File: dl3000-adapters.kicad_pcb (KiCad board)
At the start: 2 copper layers, 57 x 68 mm, 7 parts, among them J1 Banana Jack, J2 BNC, J3 Banana Jack

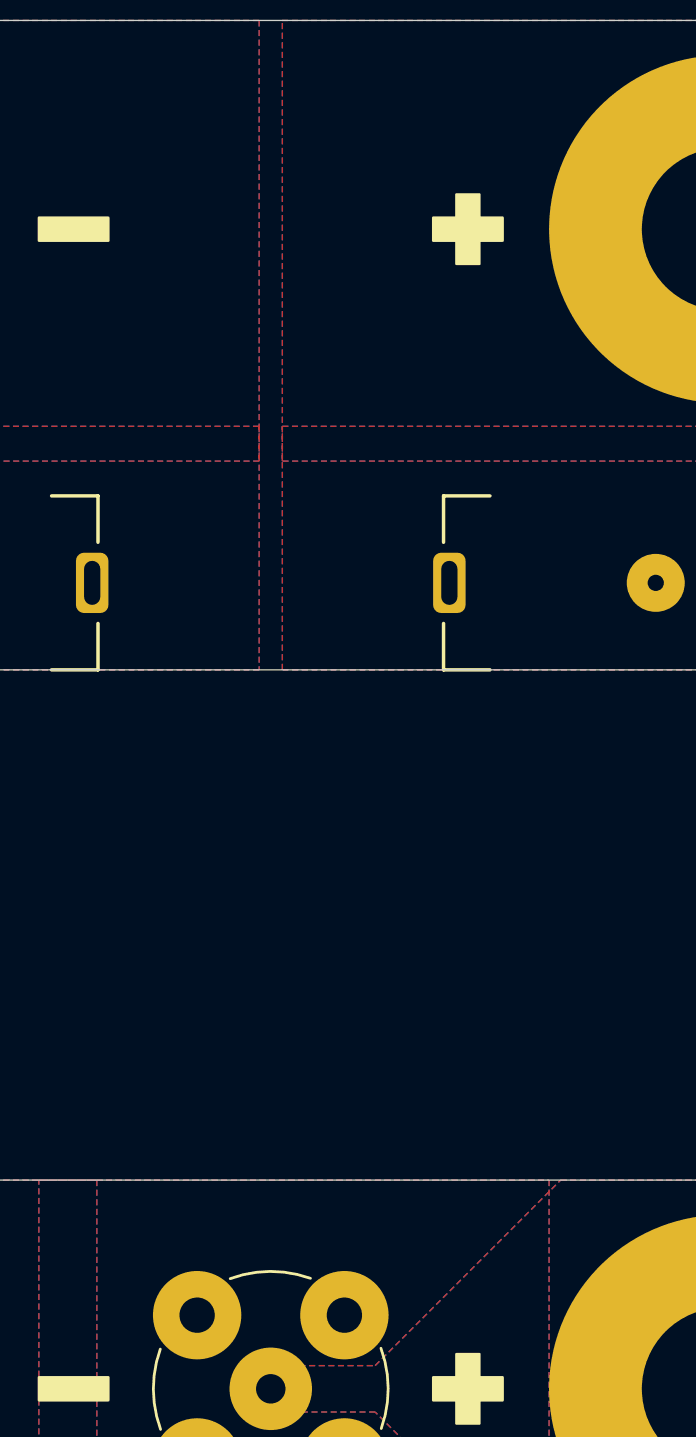
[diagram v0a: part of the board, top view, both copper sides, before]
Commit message: Add high voltage symbols to top silk screen
This includes deriving the very small and ultra small symbol from the
copper layer variant already present in the library.
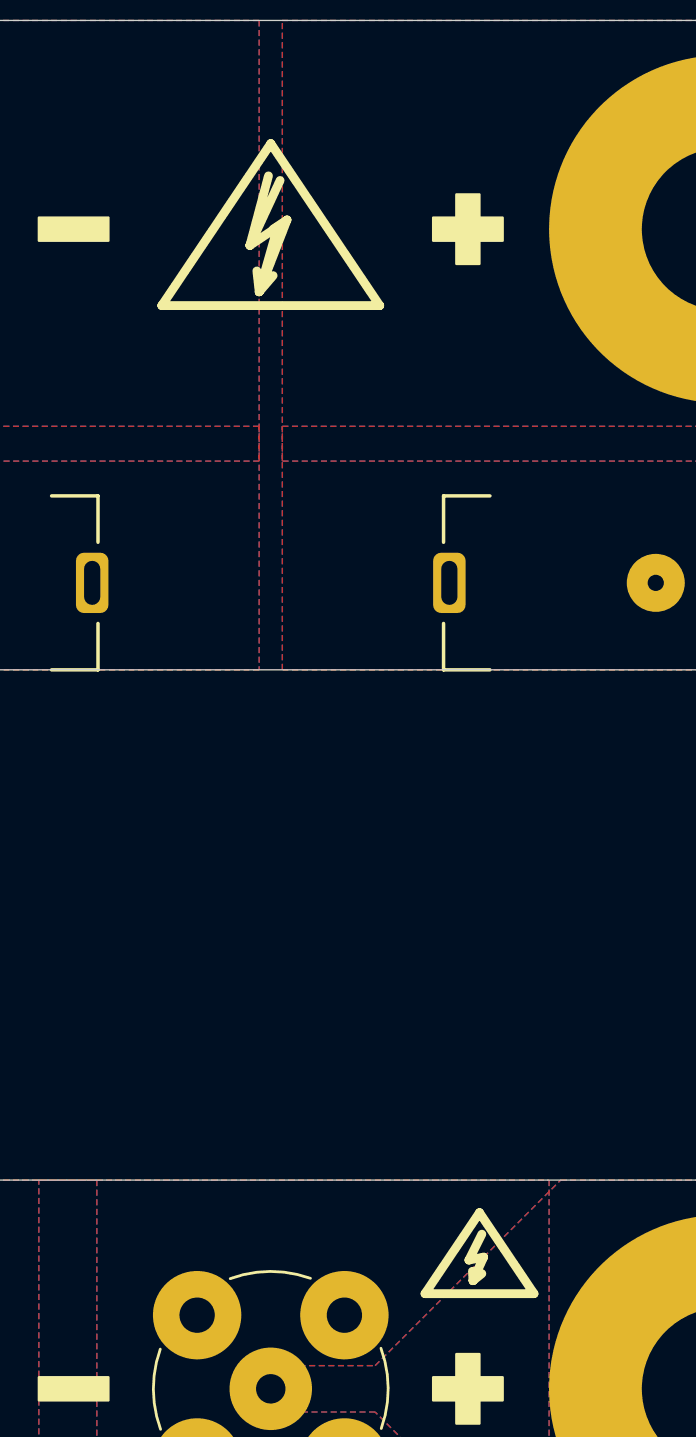
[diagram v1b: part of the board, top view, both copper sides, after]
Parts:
- added REF**: Symbol_HighVoltage_Type2_SilkScreenTop_UltraSmall, Symbol_Local:Symbol_HighVoltage_Type2_SilkScreenTop_UltraSmall, F.Cu at (159.0, 94.5)
- added REF**: Symbol_HighVoltage_Type2_SilkScreenTop_VerySmall, Symbol_Local:Symbol_HighVoltage_Type2_SilkScreenTop_VerySmall, F.Cu at (150.0, 50.5)
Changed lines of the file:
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@@
     (tracks 0)
     (zones 0)
-    (modules 7)
+    (modules 9)
     (nets 5)
   )
@@
     (add_net /BANANA+)
     (add_net /BNC+)
+  )
+  (module Symbol_Local:Symbol_HighVoltage_Type2_SilkScreenTop_UltraSmall (layer F.Cu)
+    (at 159 94.5)
+    (descr "Symbol, High Voltage, Type 2, Copper Top, Very Small,")
+    (tags "Symbol, High Voltage, Type 2, Copper Top, Very Small,")
+    (attr virtual)
+    (fp_text reference REF** (at -0.127 -5.715) (layer F.SilkS) hide
+      (effects (font (size 1 1) (thickness 0.15)))
+    )
+    (fp_text value Symbol_HighVoltage_Type2_SilkScreenTop_UltraSmall (at -0.381 4.572) (layer F.Fab) hide
+      (effects (font (size 1 1) (thickness 0.15)))
+    )
+    (fp_line (start -0.2794 0.8382) (end 0.1016 0.5334) (layer F.SilkS) (width 0.381))
+    (fp_line (start -0.3048 0.4318) (end -0.2794 0.8382) (layer F.SilkS) (width 0.381))
+    (fp_line (start 0.1778 -0.1778) (end -0.2794 0.8382) (layer F.SilkS) (width 0.381))
+    (fp_line (start -0.4572 -0.0508) (end 0.1778 -0.1778) (layer F.SilkS) (width 0.381))
+    (fp_line (start 0.1016 -1.1684) (end -0.4572 -0.0508) (layer F.SilkS) (width 0.381))
+    (fp_line (start 0 -2.0955) (end 2.3495 1.397) (layer F.SilkS) (width 0.381))
+    (fp_line (start 2.3495 1.397) (end -2.3495 1.397) (layer F.SilkS) (width 0.381))
+    (fp_line (start -2.3495 1.397) (end 0 -2.0955) (layer F.SilkS) (width 0.381))
+  )
+  (module Symbol_Local:Symbol_HighVoltage_Type2_SilkScreenTop_VerySmall (layer F.Cu)
+    (at 150 50.5)
+    (descr "Symbol, High Voltage, Type 2, Copper Top, Very Small,")
+    (tags "Symbol, High Voltage, Type 2, Copper Top, Very Small,")
+    (attr virtual)
+    (fp_text reference REF** (at -0.127 -5.715) (layer F.SilkS) hide
+      (effects (font (size 1 1) (thickness 0.15)))
+    )
+    (fp_text value Symbol_HighVoltage_Type2_SilkScreenTop_VerySmall (at -0.381 4.572) (layer F.Fab) hide
+      (effects (font (size 1 1) (thickness 0.15)))
+    )
+    (fp_line (start -0.49784 2.19964) (end 0.70104 -0.89916) (layer F.SilkS) (width 0.381))
+    (fp_line (start 0.70104 -0.89916) (end 0.1016 -0.50038) (layer F.SilkS) (width 0.381))
+    (fp_line (start -0.89916 0.20066) (end 0.40132 -2.60096) (layer F.SilkS) (width 0.381))
+    (fp_line (start -0.49784 2.19964) (end 0.1016 1.50114) (layer F.SilkS) (width 0.381))
+    (fp_line (start -0.09906 -2.79908) (end -0.89916 0.20066) (layer F.SilkS) (width 0.381))
+    (fp_line (start -0.89916 0.20066) (end 0.29972 -0.59944) (layer F.SilkS) (width 0.381))
+    (fp_line (start 0.29972 -0.59944) (end -0.49784 2.19964) (layer F.SilkS) (width 0.381))
+    (fp_line (start -0.49784 2.19964) (end -0.59944 1.30048) (layer F.SilkS) (width 0.381))
+    (fp_line (start 0 -4.191) (end 4.699 2.794) (layer F.SilkS) (width 0.381))
+    (fp_line (start 4.699 2.794) (end -4.699 2.794) (layer F.SilkS) (width 0.381))
+    (fp_line (start -4.699 2.794) (end 0 -4.191) (layer F.SilkS) (width 0.381))
   )
   (module Symbol:OSHW-Logo_5.7x6mm_SilkScreen (layer B.Cu)
@@
       (effects (font (size 1 1) (thickness 0.15)))
     )
-    (fp_text value "Banana Jack" (at -2.75 8 180) (layer F.Fab)
+    (fp_text value "Banana Jack" (at -2.75 8 180) (layer F.Fab) hide
       (effects (font (size 1 1) (thickness 0.15)))
     )
@@
       (effects (font (size 1 1) (thickness 0.15)))
     )
-    (fp_text value BNC (at 0 6.5) (layer F.Fab)
+    (fp_text value BNC (at 0 6.5) (layer F.Fab) hide
       (effects (font (size 1 1) (thickness 0.15)))
     )
@@
       (effects (font (size 1 1) (thickness 0.15)))
     )
-    (fp_text value "Banana Jack" (at 2.75 7 180) (layer F.Fab)
+    (fp_text value "Banana Jack" (at 2.75 7 180) (layer F.Fab) hide
       (effects (font (size 1 1) (thickness 0.15)))
     )
@@
       (effects (font (size 1 1) (thickness 0.15)))
     )
-    (fp_text value "Binding Posts" (at 0 8.5) (layer F.Fab)
+    (fp_text value "Binding Posts" (at 0 8.5) (layer F.Fab) hide
       (effects (font (size 1 1) (thickness 0.15)))
     )
@@
       (effects (font (size 1 1) (thickness 0.15)))
     )
-    (fp_text value "Binding Posts" (at 0 12.7) (layer F.Fab)
-      (effects (font (size 1 1) (thickness 0.15)))
-    )
+    (fp_text value "Binding Posts" (at 0 12.7) (layer F.Fab) hide
+      (effects (font (size 1 1) (thickness 0.15)))
+    )

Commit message: pomona footprint
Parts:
- added J4: Banana Jack, Connector_Local:Pomona_73099, F.Cu at (139.2, 65.3)
- added J5: Banana Jack, Connector_Local:Pomona_73099, F.Cu at (154.3, 65.3)
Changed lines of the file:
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@@
-(kicad_pcb (version 20171130) (host pcbnew "(5.1.5-0-10_14)")
+(kicad_pcb (version 20171130) (host pcbnew "(5.1.8)-1")
   (general
     (thickness 1.6)
@@
     (tracks 0)
     (zones 0)
-    (modules 9)
+    (modules 11)
     (nets 5)
   )
@@
   (layers
     (0 F.Cu signal)
-    (31 B.Cu signal)
-    (32 B.Adhes user)
-    (33 F.Adhes user)
-    (34 B.Paste user)
-    (35 F.Paste user)
-    (36 B.SilkS user)
+    (31 B.Cu signal hide)
+    (32 B.Adhes user hide)
+    (33 F.Adhes user hide)
+    (34 B.Paste user hide)
+    (35 F.Paste user hide)
+    (36 B.SilkS user hide)
     (37 F.SilkS user)
-    (38 B.Mask user)
+    (38 B.Mask user hide)
     (39 F.Mask user)
     (40 Dwgs.User user)
-    (41 Cmts.User user)
-    (42 Eco1.User user)
-    (43 Eco2.User user)
+    (41 Cmts.User user hide)
+    (42 Eco1.User user hide)
+    (43 Eco2.User user hide)
     (44 Edge.Cuts user)
-    (45 Margin user)
-    (46 B.CrtYd user)
-    (47 F.CrtYd user)
-    (48 B.Fab user)
-    (49 F.Fab user)
+    (45 Margin user hide)
+    (46 B.CrtYd user hide)
+    (47 F.CrtYd user hide)
+    (48 B.Fab user hide)
+    (49 F.Fab user hide)
   )
   (setup
@@
     (solder_mask_min_width 0.1016)
     (aux_axis_origin 0 0)
-    (visible_elements FFFFF77F)
+    (visible_elements 7FFFFFFF)
     (pcbplotparams
       (layerselection 0x010fc_ffffffff)
@@
     (add_net /BANANA+)
     (add_net /BNC+)
+  )
+  (module Connector_Local:Pomona_73099 (layer F.Cu)
+    (at 154.305 65.278)
+    (fp_text reference J5 (at 1 -4) (layer F.SilkS)
+      (effects (font (size 1 1) (thickness 0.15)))
+    )
+    (fp_text value "Banana Jack" (at 1 3) (layer F.Fab)
+      (effects (font (size 1 1) (thickness 0.15)))
+    )
+    (fp_line (start 28.5 7) (end 28.5 -7) (layer F.CrtYd) (width 0.12))
+    (fp_line (start -6.5 -7) (end -6.5 7) (layer F.CrtYd) (width 0.12))
+    (fp_line (start -6.5 7) (end 28.5 7) (layer F.CrtYd) (width 0.12))
+    (fp_line (start 28.5 -7) (end -6.5 -7) (layer F.CrtYd) (width 0.12))
+    (fp_line (start 27.5 -6) (end -5.5 -6) (layer Dwgs.User) (width 0.12))
+    (fp_line (start 27.5 6) (end 27.5 -6) (layer Dwgs.User) (width 0.12))
+    (fp_line (start -5.5 6) (end 27.5 6) (layer Dwgs.User) (width 0.12))
+    (fp_line (start -5.5 -6) (end -5.5 6) (layer Dwgs.User) (width 0.12))
+    (pad "" thru_hole circle (at -4.09 5.08) (size 2 2) (drill 1.3) (layers *.Cu *.Mask))
+    (pad "" thru_hole circle (at 6.36 5.08) (size 2 2) (drill 1.3) (layers *.Cu *.Mask))
+    (pad "" thru_hole circle (at 6.36 -5.09) (size 2 2) (drill 1.3) (layers *.Cu *.Mask))
+    (pad "" thru_hole circle (at -3.8 -5.08) (size 2 2) (drill 1.3) (layers *.Cu *.Mask))
+    (pad 1 thru_hole circle (at 0 0) (size 4 4) (drill 2.2) (layers *.Cu *.Mask)
+      (net 4 /BANANA+))
+  )
+  (module Connector_Local:Pomona_73099 (layer F.Cu)
+    (at 139.192 65.278 180)
+    (fp_text reference J4 (at 1 -4) (layer F.SilkS)
+      (effects (font (size 1 1) (thickness 0.15)))
+    )
+    (fp_text value "Banana Jack" (at 1 3) (layer F.Fab)
+      (effects (font (size 1 1) (thickness 0.15)))
+    )
+    (fp_line (start 28.5 7) (end 28.5 -7) (layer F.CrtYd) (width 0.12))
+    (fp_line (start -6.5 -7) (end -6.5 7) (layer F.CrtYd) (width 0.12))
+    (fp_line (start -6.5 7) (end 28.5 7) (layer F.CrtYd) (width 0.12))
+    (fp_line (start 28.5 -7) (end -6.5 -7) (layer F.CrtYd) (width 0.12))
+    (fp_line (start 27.5 -6) (end -5.5 -6) (layer Dwgs.User) (width 0.12))
+    (fp_line (start 27.5 6) (end 27.5 -6) (layer Dwgs.User) (width 0.12))
+    (fp_line (start -5.5 6) (end 27.5 6) (layer Dwgs.User) (width 0.12))
+    (fp_line (start -5.5 -6) (end -5.5 6) (layer Dwgs.User) (width 0.12))
+    (pad "" thru_hole circle (at -4.09 5.08 180) (size 2 2) (drill 1.3) (layers *.Cu *.Mask))
+    (pad "" thru_hole circle (at 6.36 5.08 180) (size 2 2) (drill 1.3) (layers *.Cu *.Mask))
+    (pad "" thru_hole circle (at 6.36 -5.09 180) (size 2 2) (drill 1.3) (layers *.Cu *.Mask))
+    (pad "" thru_hole circle (at -3.8 -5.08 180) (size 2 2) (drill 1.3) (layers *.Cu *.Mask))
+    (pad 1 thru_hole circle (at 0 0 180) (size 4 4) (drill 2.2) (layers *.Cu *.Mask)
+      (net 1 /BANANA-))
   )
   (module Symbol_Local:Symbol_HighVoltage_Type2_SilkScreenTop_UltraSmall (layer F.Cu)
@@
     (fp_line (start 1 17.55) (end 1 18.05) (layer F.Fab) (width 0.1))
     (fp_line (start 3.75 -2.95) (end -3.75 -2.95) (layer F.Fab) (width 0.1))
-    (fp_text user "PCB Edge" (at 0 -2 90) (layer Dwgs.User)
-      (effects (font (size 1 1) (thickness 0.15)))
-    )
     (fp_line (start -3.75 -2.95) (end -3.75 -1.95) (layer F.Fab) (width 0.1))
     (fp_line (start 3.75 -0.95) (end 3.75 16.05) (layer F.Fab) (width 0.1))
+    (fp_text user "PCB Edge" (at 0 -2 90) (layer Dwgs.User)
+      (effects (font (size 1 1) (thickness 0.15)))
+    )
     (pad "" np_thru_hole circle (at 0 8.9) (size 2.5 2.5) (drill 0.7) (layers *.Cu *.Mask))
     (pad 1 thru_hole roundrect (at 0 17.8) (size 1.4 2.6) (drill oval 0.7 1.9) (layers *.Cu *.Mask) (roundrect_rratio 0.25)
@@
       (effects (font (size 1 1) (thickness 0.15)))
     )
-    (fp_text user %R (at 0 0) (layer F.Fab)
-      (effects (font (size 1 1) (thickness 0.15)))
-    )
     (fp_line (start 5.5 -5.5) (end 5.5 5.5) (layer F.CrtYd) (width 0.05))
     (fp_line (start 5.5 5.5) (end -5.5 5.5) (layer F.CrtYd) (width 0.05))
@@
     (fp_line (start -5.5 -5.5) (end 5.5 -5.5) (layer F.CrtYd) (width 0.05))
     (fp_circle (center 0 0) (end 4.8 0) (layer F.Fab) (width 0.1))
+    (fp_text user %R (at 0 0) (layer F.Fab)
+      (effects (font (size 1 1) (thickness 0.15)))
+    )
     (fp_arc (start 0 0) (end -4.75 1.75) (angle 40) (layer F.SilkS) (width 0.12))
     (fp_arc (start 0 0) (end 1.75 4.75) (angle 40) (layer F.SilkS) (width 0.12))
@@
     (fp_line (start 3.75 -0.95) (end 3.75 16.05) (layer F.Fab) (width 0.1))
     (fp_line (start -3.75 -2.95) (end -3.75 -1.95) (layer F.Fab) (width 0.1))
-    (fp_text user "PCB Edge" (at 0 -2 90) (layer Dwgs.User)
-      (effects (font (size 1 1) (thickness 0.15)))
-    )
     (fp_line (start 3.75 -2.95) (end -3.75 -2.95) (layer F.Fab) (width 0.1))
     (fp_line (start 1 17.55) (end 1 18.05) (layer F.Fab) (width 0.1))
@@
     (fp_line (start 3.75 17.05) (end 4.25 17.05) (layer F.Fab) (width 0.1))
     (fp_line (start 3.75 17.05) (end 3.75 18.05) (layer F.Fab) (width 0.1))
+    (fp_text user "PCB Edge" (at 0 -2 90) (layer Dwgs.User)
+      (effects (font (size 1 1) (thickness 0.15)))
+    )
     (pad 1 thru_hole roundrect (at 0 0 180) (size 1.4 2.6) (drill oval 0.7 1.9) (layers *.Cu *.Mask) (roundrect_rratio 0.25)
       (net 4 /BANANA+))
@@
     )
     (fp_line (start -19.5 -10) (end 19.5 -10) (layer F.CrtYd) (width 0.12))
-    (fp_arc (start -19.5 0) (end -19.5 -10) (angle -180) (layer F.CrtYd) (width 0.12))
-    (fp_arc (start 19.5 0) (end 19.5 10) (angle -180) (layer F.CrtYd) (width 0.12))
     (fp_line (start -19.5 10) (end 19.5 10) (layer F.CrtYd) (width 0.12))
     (fp_poly (pts (xy 9 -0.5) (xy 10 -0.5) (xy 10 0.5) (xy 9 0.5)
@@
       (xy 7 -0.5) (xy 8 -0.5) (xy 8 -1.5) (xy 9 -1.5)) (layer F.SilkS) (width 0.1))
     (fp_poly (pts (xy -7 0.5) (xy -10 0.5) (xy -10 -0.5) (xy -7 -0.5)) (layer F.SilkS) (width 0.1))
+    (fp_arc (start -19.5 0) (end -19.5 -10) (angle -180) (layer F.CrtYd) (width 0.12))
+    (fp_arc (start 19.5 0) (end 19.5 10) (angle -180) (layer F.CrtYd) (width 0.12))
     (pad 1 thru_hole circle (at -19.5 0) (size 15 15) (drill 7) (layers *.Cu *.Mask)
       (net 1 /BANANA-))
@@
       (xy 7 -0.5) (xy 8 -0.5) (xy 8 -1.5) (xy 9 -1.5)) (layer F.SilkS) (width 0.1))
     (fp_line (start -19.5 10) (end 19.5 10) (layer F.CrtYd) (width 0.12))
+    (fp_line (start -19.5 -10) (end 19.5 -10) (layer F.CrtYd) (width 0.12))
     (fp_arc (start 19.5 0) (end 19.5 10) (angle -180) (layer F.CrtYd) (width 0.12))
     (fp_arc (start -19.5 0) (end -19.5 -10) (angle -180) (layer F.CrtYd) (width 0.12))
-    (fp_line (start -19.5 -10) (end 19.5 -10) (layer F.CrtYd) (width 0.12))
     (pad 2 thru_hole circle (at 19.5 0) (size 15 15) (drill 7) (layers *.Cu *.Mask)
       (net 3 /BNC+))
